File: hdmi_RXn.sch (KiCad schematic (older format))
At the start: 40 parts

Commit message: Fix issues due to different KiCad version
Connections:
- wire segments 205 -> 169

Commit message: Fix caps issues in templates
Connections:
- wire segments 169 -> 171
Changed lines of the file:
@@
 LIBS:hdmi2usb
 LIBS:HDMI2USB-cache
-LIBS:HDMI2USB-pcie-artix7-cache
 EELAYER 25 0
 EELAYER END
 $Descr A3 16535 11693
 encoding utf-8
-Sheet 8 14
+Sheet 1 1
 Title ""
 Date ""
@@
 Wire Wire Line
 	6300 5450 6300 5550
+Wire Wire Line
+	2050 3100 2050 3150
+Wire Wire Line
+	2650 1400 2650 1450
 $EndSCHEMATC

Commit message: Annotate HDMI RX template.
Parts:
- gave numbers to parts that had none: 40

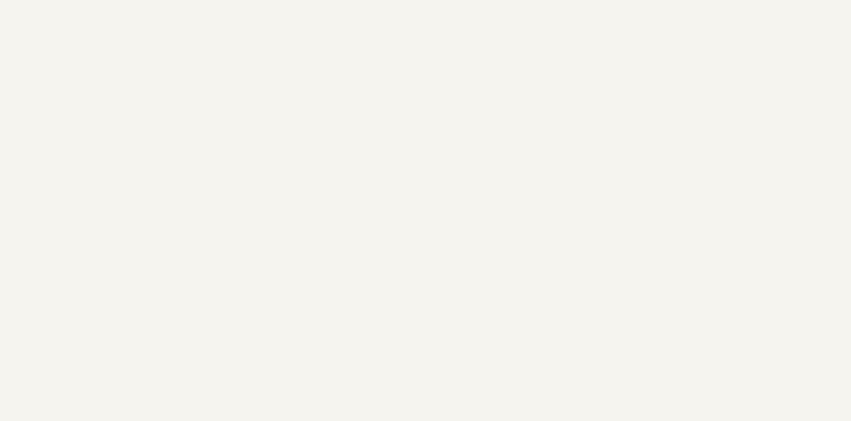
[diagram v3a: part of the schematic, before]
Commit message: Adding warning text.
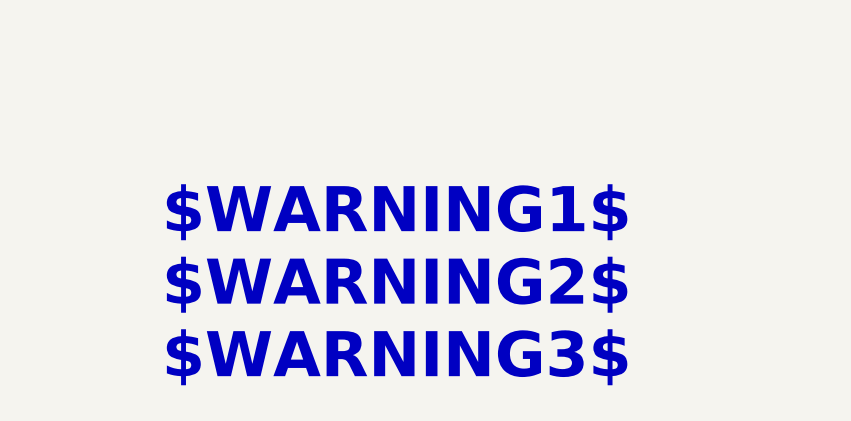
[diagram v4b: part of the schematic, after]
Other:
- note added: "$WARNING1$\n$WARNING2$\n$WARNING3$"
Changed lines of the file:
@@
 LIBS:hdmi2usb
 LIBS:HDMI2USB-cache
+LIBS:hdmi_RXn-cache
 EELAYER 25 0
 EELAYER END
@@
 Wire Wire Line
 	2650 1400 2650 1450
+Text Notes 9945 8285 0    197  ~ 39
+$WARNING1$\n$WARNING2$\n$WARNING3$
 $EndSCHEMATC

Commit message: Add CEC to HDMI headers.
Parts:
- removed P1: CONN_5, symbol CONN_5
- added P1: CONN_01X06, symbol CONN_01X06
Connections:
- wire segments 171 -> 172
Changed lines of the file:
@@
 Text HLabel 6050 5000 0    60   Input ~ 0
 HDMI_$RXn$_PEEN
-$Comp
-L CONN_5 P1
-U 1 1 57C4CA07
-P 6150 6900
-F 0 "P1" V 6100 6900 50  0000 C CNN
-F 1 "CONN_5" V 6200 6900 50  0000 C CNN
-F 2 "" H 6150 6900 60  0000 C CNN
-F 3 "" H 6150 6900 60  0000 C CNN
-	1    6150 6900
-	1    0    0    -1
-$EndComp
 Text Label 4950 6700 0    60   ~ 0
 HDMI_$RXn$_SCL
 Text Label 4950 6800 0    60   ~ 0
 HDMI_$RXn$_SDA
+Text Label 5300 7100 0    60   ~ 0
+VCC3V3
 Text Label 5300 7000 0    60   ~ 0
-VCC3V3
-Text Label 5300 7100 0    60   ~ 0
 GND
 $Comp
@@
 Text Notes 9945 8285 0    197  ~ 39
 $WARNING1$\n$WARNING2$\n$WARNING3$
+$Comp
+L CONN_01X06 P1
+U 1 1 57D665F8
+P 5950 6850
+F 0 "P1" H 6028 6891 50  0000 L CNN
+F 1 "CONN_01X06" H 6028 6800 50  0000 L CNN
+F 2 "" H 5950 6850 50  0000 C CNN
+F 3 "" H 5950 6850 50  0000 C CNN
+	1    5950 6850
+	1    0    0    -1
+$EndComp
+Wire Wire Line
+	5750 6600 4950 6600
+Text Label 4950 6600 0    60   ~ 0
+HDMI_$RXn$_CEC
 $EndSCHEMATC

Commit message: Adding more to the debug header (making it PMOD compatible).
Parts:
- removed P1: CONN_01X06, symbol CONN_01X06
- added P$RXn$1: CONN_02X06, symbol CONN_02X06
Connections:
- net labels added: HDMI_$RXn$_IO0, HDMI_$RXn$_IO1
- wire segments 172 -> 184
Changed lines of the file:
@@
 Text Notes 9945 8285 0    197  ~ 39
 $WARNING1$\n$WARNING2$\n$WARNING3$
-$Comp
-L CONN_01X06 P1
-U 1 1 57D665F8
-P 5950 6850
-F 0 "P1" H 6028 6891 50  0000 L CNN
-F 1 "CONN_01X06" H 6028 6800 50  0000 L CNN
-F 2 "" H 5950 6850 50  0000 C CNN
-F 3 "" H 5950 6850 50  0000 C CNN
-	1    5950 6850
-	1    0    0    -1
-$EndComp
 Wire Wire Line
 	5750 6600 4950 6600
 Text Label 4950 6600 0    60   ~ 0
 HDMI_$RXn$_CEC
+$Comp
+L CONN_02X06 P$RXn$1
+U 1 1 57D66065
+P 6000 6850
+F 0 "P$RXn$1" H 6000 7315 50  0000 C CNN
+F 1 "CONN_02X06" H 6000 7224 50  0000 C CNN
+F 2 "" H 6000 5650 50  0000 C CNN
+F 3 "" H 6000 5650 50  0000 C CNN
+	1    6000 6850
+	1    0    0    -1
+$EndComp
+Wire Wire Line
+	5690 7000 5690 7220
+Wire Wire Line
+	5690 7220 6340 7220
+Wire Wire Line
+	6340 7220 6340 7000
+Wire Wire Line
+	6340 7000 6250 7000
+Connection ~ 5690 7000
+Wire Wire Line
+	5650 7100 5650 7285
+Wire Wire Line
+	5650 7285 6290 7285
+Connection ~ 5650 7100
+Text Label 7050 6700 2    60   ~ 0
+HDMI_$RXn$_IO1
+Text Label 7050 6800 2    60   ~ 0
+HDMI_$RXn$_TXEN
+Text Label 7050 6900 2    60   ~ 0
+HDMI_$RXn$_PEEN
+Wire Wire Line
+	6250 6700 7050 6700
+Wire Wire Line
+	6250 6800 7050 6800
+Wire Wire Line
+	6250 6900 7050 6900
+Wire Wire Line
+	7050 6600 6250 6600
+Text Label 7050 6600 2    60   ~ 0
+HDMI_$RXn$_IO0
+Text HLabel 7050 6600 2    60   BiDi ~ 0
+HDMI_$RXn$_IO0
+Text HLabel 7050 6700 2    60   BiDi ~ 0
+HDMI_$RXn$_IO1
+Wire Wire Line
+	6290 7285 6290 7100
+Wire Wire Line
+	6290 7100 6250 7100
 $EndSCHEMATC

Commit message: Adding footprints to hdmi_RXn schematic.
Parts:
- C$RXn$1, C$RXn$10, C$RXn$11, C$RXn$12, C$RXn$13, C$RXn$14, C$RXn$15, C$RXn$2, C$RXn$3, C$RXn$4, C$RXn$5, C$RXn$6, C$RXn$7, C$RXn$8, C$RXn$9: footprint (none) -> Capacitors_SMD:C_0402
- J$RXn$1: manf# (none) -> 10029449-001RLF
- P$RXn$1: footprint (none) -> Pin_Headers:Pin_Header_Straight_2x06
- R$RXn$1, R$RXn$10, R$RXn$11, R$RXn$12, R$RXn$2, R$RXn$3, R$RXn$4, R$RXn$5, R$RXn$6, R$RXn$7, R$RXn$8, R$RXn$9: footprint (none) -> Resistors_SMD:R_0402
- U$RXn$1: footprint (none) -> Housings_DFN_QFN:QFN-40-1EP_6x6mm_Pitch0.5mm; manf# (none) -> AD8195ACPZ
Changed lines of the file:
@@
 F 0 "U$RXn$1" H 8700 1700 60  0000 C CNN
 F 1 "AD8195" H 8050 2950 60  0000 C CNN
-F 2 "" H 8000 2850 60  0000 C CNN
+F 2 "Housings_DFN_QFN:QFN-40-1EP_6x6mm_Pitch0.5mm" H 8000 2850 60  0001 C CNN
 F 3 "" H 8000 2850 60  0000 C CNN
+F 4 "AD8195ACPZ" H 8050 2850 60  0001 C CNN "manf#"
 	1    8050 2850
 	1    0    0    -1
@@
 F 0 "J$RXn$1" H 4600 4050 60  0000 C CNN
 F 1 "HDMI" V 4900 3000 60  0000 C CNN
-F 2 "" H 4700 3000 60  0000 C CNN
+F 2 "" H 4700 3000 60  0001 C CNN
 F 3 "" H 4700 3000 60  0000 C CNN
+F 4 "10029449-001RLF" H 4750 3000 60  0001 C CNN "manf#"
 	1    4750 3000
 	-1   0    0    -1
@@
 F 0 "R$RXn$5" V 5730 3100 50  0000 C CNN
 F 1 "R" V 5657 3101 50  0000 C CNN
-F 2 "" V 5580 3100 30  0000 C CNN
+F 2 "Resistors_SMD:R_0402" V 5580 3100 30  0001 C CNN
 F 3 "" H 5650 3100 30  0000 C CNN
 	1    5650 3100
@@
 F 0 "D$RXn$2" H 6550 1050 50  0000 C CNN
 F 1 "DIODE" H 6750 950 50  0000 C CNN
-F 2 "" H 6550 950 60  0000 C CNN
+F 2 "" H 6550 950 60  0001 C CNN
 F 3 "" H 6550 950 60  0000 C CNN
 	1    6550 950
@@
 F 0 "D$RXn$3" H 6550 1050 50  0000 C CNN
 F 1 "DIODE" H 6750 1150 50  0000 C CNN
-F 2 "" H 6550 1150 60  0000 C CNN
+F 2 "" H 6550 1150 60  0001 C CNN
 F 3 "" H 6550 1150 60  0000 C CNN
 	1    6550 1150
@@
 $EndComp
 $Comp
-L GND #PWR2
+L GND #PWR01
 U 1 1 57C0819F
 P 7850 4300
-F 0 "#PWR2" H 7850 4050 60  0001 C CNN
+F 0 "#PWR01" H 7850 4050 60  0001 C CNN
 F 1 "GND" H 7850 4150 60  0000 C CNN
 F 2 "" H 7850 4300 60  0000 C CNN
@@
 F 0 "C$RXn$15" H 9100 4100 50  0000 L CNN
 F 1 "C" H 9100 3900 50  0000 L CNN
-F 2 "" H 9088 3850 30  0000 C CNN
+F 2 "Capacitors_SMD:C_0402" H 9088 3850 30  0001 C CNN
 F 3 "" H 9050 4000 60  0000 C CNN
 	1    9050 4000
@@
 F 0 "C$RXn$13" H 6300 1500 50  0000 L CNN
 F 1 "C" H 6800 1400 50  0000 L CNN
-F 2 "" H 6788 1350 30  0000 C CNN
+F 2 "Capacitors_SMD:C_0402" H 6788 1350 30  0001 C CNN
 F 3 "" H 6750 1500 60  0000 C CNN
 	1    6750 1500
@@
 F 0 "C$RXn$14" H 7000 1600 50  0000 L CNN
 F 1 "C" H 7000 1400 50  0000 L CNN
-F 2 "" H 6988 1350 30  0000 C CNN
+F 2 "Capacitors_SMD:C_0402" H 6988 1350 30  0001 C CNN
 F 3 "" H 6950 1500 60  0000 C CNN
 	1    6950 1500
@@
 $EndComp
 $Comp
-L GND #PWR1
+L GND #PWR02
 U 1 1 57C093D2
 P 6850 1800
-F 0 "#PWR1" H 6850 1550 60  0001 C CNN
+F 0 "#PWR02" H 6850 1550 60  0001 C CNN
 F 1 "GND" H 6850 1650 60  0000 C CNN
 F 2 "" H 6850 1800 60  0000 C CNN
@@
 F 0 "R$RXn$9" V 10280 4600 50  0000 C CNN
 F 1 "47K" V 10207 4601 50  0000 C CNN
-F 2 "" V 10130 4600 30  0000 C CNN
+F 2 "Resistors_SMD:R_0402" V 10130 4600 30  0001 C CNN
 F 3 "" H 10200 4600 30  0000 C CNN
 	1    10200 4600
@@
 F 0 "R$RXn$11" V 10430 4600 50  0000 C CNN
 F 1 "47K" V 10357 4601 50  0000 C CNN
-F 2 "" V 10280 4600 30  0000 C CNN
+F 2 "Resistors_SMD:R_0402" V 10280 4600 30  0001 C CNN
 F 3 "" H 10350 4600 30  0000 C CNN
 	1    10350 4600
@@
 F 0 "R$RXn$10" V 10280 5750 50  0000 C CNN
 F 1 "1K" V 10207 5751 50  0000 C CNN
-F 2 "" V 10130 5750 30  0000 C CNN
+F 2 "Resistors_SMD:R_0402" V 10130 5750 30  0001 C CNN
 F 3 "" H 10200 5750 30  0000 C CNN
 	1    10200 5750
@@
 F 0 "R$RXn$12" V 10430 5750 50  0000 C CNN
 F 1 "1K" V 10357 5751 50  0000 C CNN
-F 2 "" V 10280 5750 30  0000 C CNN
+F 2 "Resistors_SMD:R_0402" V 10280 5750 30  0001 C CNN
 F 3 "" H 10350 5750 30  0000 C CNN
 	1    10350 5750
@@
 $EndComp
 $Comp
-L VCC3V3 #PWR3
+L VCC3V3 #PWR03
 U 1 1 57C0DF7C
 P 10200 5300
-F 0 "#PWR3" H 10200 5150 60  0001 C CNN
+F 0 "#PWR03" H 10200 5150 60  0001 C CNN
 F 1 "VCC3V3" H 10200 5440 60  0000 C CNN
 F 2 "" H 10200 5300 60  0000 C CNN
@@
 F 0 "FB$RXn$4" H 5700 3900 50  0000 C CNN
 F 1 "FILTER" H 5700 3700 50  0000 C CNN
-F 2 "" H 5700 3800 60  0000 C CNN
+F 2 "" H 5700 3800 60  0001 C CNN
 F 3 "" H 5700 3800 60  0000 C CNN
 	1    5700 3800
@@
 F 0 "FB$RXn$2" H 1650 2000 50  0000 C CNN
 F 1 "FILTER" H 1650 1750 50  0000 C CNN
-F 2 "" H 1650 1850 60  0000 C CNN
+F 2 "" H 1650 1850 60  0001 C CNN
 F 3 "" H 1650 1850 60  0000 C CNN
 	1    1650 1850
@@
 F 0 "C$RXn$2" H 1700 2250 50  0000 L CNN
 F 1 "10uF" H 2100 2050 50  0000 L CNN
-F 2 "" H 2088 2000 30  0000 C CNN
+F 2 "Capacitors_SMD:C_0402" H 2088 2000 30  0001 C CNN
 F 3 "" H 2050 2150 60  0000 C CNN
 	1    2050 2150
@@
 F 0 "C$RXn$5" H 2200 2250 50  0000 L CNN
 F 1 "0.1uF" H 2400 2050 50  0000 L CNN
-F 2 "" H 2388 2000 30  0000 C CNN
+F 2 "Capacitors_SMD:C_0402" H 2388 2000 30  0001 C CNN
 F 3 "" H 2350 2150 60  0000 C CNN
 	1    2350 2150
@@
 F 0 "C$RXn$8" H 2700 2250 50  0000 L CNN
 F 1 "10nF" H 2700 2050 50  0000 L CNN
-F 2 "" H 2688 2000 30  0000 C CNN
+F 2 "Capacitors_SMD:C_0402" H 2688 2000 30  0001 C CNN
 F 3 "" H 2650 2150 60  0000 C CNN
 	1    2650 2150
@@
 F 0 "C$RXn$3" H 1700 3050 50  0000 L CNN
 F 1 "10uF" H 2100 2850 50  0000 L CNN
-F 2 "" H 2088 2800 30  0000 C CNN
+F 2 "Capacitors_SMD:C_0402" H 2088 2800 30  0001 C CNN
 F 3 "" H 2050 2950 60  0000 C CNN
 	1    2050 2950
@@
 F 0 "C$RXn$6" H 2200 3050 50  0000 L CNN
 F 1 "0.1uF" H 2400 2850 50  0000 L CNN
-F 2 "" H 2388 2800 30  0000 C CNN
+F 2 "Capacitors_SMD:C_0402" H 2388 2800 30  0001 C CNN
 F 3 "" H 2350 2950 60  0000 C CNN
 	1    2350 2950
@@
 F 0 "C$RXn$9" H 2700 3050 50  0000 L CNN
 F 1 "10nF" H 2700 2850 50  0000 L CNN
-F 2 "" H 2688 2800 30  0000 C CNN
+F 2 "Capacitors_SMD:C_0402" H 2688 2800 30  0001 C CNN
 F 3 "" H 2650 2950 60  0000 C CNN
 	1    2650 2950
@@
 F 0 "C$RXn$1" V 1950 1100 50  0000 L CNN
 F 1 "10uF" V 2100 1300 50  0000 L CNN
-F 2 "" H 2088 1100 30  0000 C CNN
+F 2 "Capacitors_SMD:C_0402" H 2088 1100 30  0001 C CNN
 F 3 "" H 2050 1250 60  0000 C CNN
 	1    2050 1250
@@
 F 0 "C$RXn$4" V 2250 1100 50  0000 L CNN
 F 1 "0.1uF" V 2400 1300 50  0000 L CNN
-F 2 "" H 2388 1100 30  0000 C CNN
+F 2 "Capacitors_SMD:C_0402" H 2388 1100 30  0001 C CNN
 F 3 "" H 2350 1250 60  0000 C CNN
 	1    2350 1250
@@
 F 0 "C$RXn$7" V 2550 1100 50  0000 L CNN
 F 1 "0.1uF" V 2700 1300 50  0000 L CNN
-F 2 "" H 2688 1100 30  0000 C CNN
+F 2 "Capacitors_SMD:C_0402" H 2688 1100 30  0001 C CNN
 F 3 "" H 2650 1250 60  0000 C CNN
 	1    2650 1250
@@
 F 0 "C$RXn$10" V 2850 1100 50  0000 L CNN
 F 1 "0.1uF" V 3000 1300 50  0000 L CNN
-F 2 "" H 2988 1100 30  0000 C CNN
+F 2 "Capacitors_SMD:C_0402" H 2988 1100 30  0001 C CNN
 F 3 "" H 2950 1250 60  0000 C CNN
 	1    2950 1250
@@
 F 0 "C$RXn$11" V 3150 1100 50  0000 L CNN
 F 1 "10nF" V 3300 1300 50  0000 L CNN
-F 2 "" H 3288 1100 30  0000 C CNN
+F 2 "Capacitors_SMD:C_0402" H 3288 1100 30  0001 C CNN
 F 3 "" H 3250 1250 60  0000 C CNN
 	1    3250 1250
@@
 F 0 "C$RXn$12" V 3450 1100 50  0000 L CNN
 F 1 "10nF" V 3600 1300 50  0000 L CNN
-F 2 "" H 3588 1100 30  0000 C CNN
+F 2 "Capacitors_SMD:C_0402" H 3588 1100 30  0001 C CNN
 F 3 "" H 3550 1250 60  0000 C CNN
 	1    3550 1250
@@
 F 0 "FB$RXn$3" H 1650 2800 50  0000 C CNN
 F 1 "FILTER" H 1650 2550 50  0000 C CNN
-F 2 "" H 1650 2650 60  0000 C CNN
+F 2 "" H 1650 2650 60  0001 C CNN
 F 3 "" H 1650 2650 60  0000 C CNN
 	1    1650 2650
@@
 F 0 "FB$RXn$1" H 1650 1100 50  0000 C CNN
 F 1 "FILTER" H 1650 850 50  0000 C CNN
-F 2 "" H 1650 950 60  0000 C CNN
+F 2 "" H 1650 950 60  0001 C CNN
 F 3 "" H 1650 950 60  0000 C CNN
 	1    1650 950
@@
 F 0 "R$RXn$6" V 6380 4700 50  0000 C CNN
 F 1 "100K" V 6307 4701 50  0000 C CNN
-F 2 "" V 6230 4700 30  0000 C CNN
+F 2 "Resistors_SMD:R_0402" V 6230 4700 30  0001 C CNN
 F 3 "" H 6300 4700 30  0000 C CNN
 	1    6300 4700
@@
 F 0 "R$RXn$7" V 6380 5300 50  0000 C CNN
 F 1 "100K" V 6307 5301 50  0000 C CNN
-F 2 "" V 6230 5300 30  0000 C CNN
+F 2 "Resistors_SMD:R_0402" V 6230 5300 30  0001 C CNN
 F 3 "" H 6300 5300 30  0000 C CNN
 	1    6300 5300
@@
 F 0 "R$RXn$8" V 6680 5300 50  0000 C CNN
 F 1 "100K" V 6607 5301 50  0000 C CNN
-F 2 "" V 6530 5300 30  0000 C CNN
+F 2 "Resistors_SMD:R_0402" V 6530 5300 30  0001 C CNN
 F 3 "" H 6600 5300 30  0000 C CNN
 	1    6600 5300
@@
 F 0 "Q$RXn$1" H 2800 6500 60  0000 C CNN
 F 1 "FDV301N" H 2800 6400 60  0000 C CNN
-F 2 "" H 2420 6575 60  0000 C CNN
+F 2 "" H 2420 6575 60  0001 C CNN
 F 3 "" H 2420 6575 60  0000 C CNN
 	1    2400 6600
@@
 F 0 "R$RXn$1" V 2180 6900 50  0000 C CNN
 F 1 "100K" V 2107 6901 50  0000 C CNN
-F 2 "" V 2030 6900 30  0000 C CNN
+F 2 "Resistors_SMD:R_0402" V 2030 6900 30  0001 C CNN
 F 3 "" H 2100 6900 30  0000 C CNN
 	1    2100 6900
@@
 F 0 "R$RXn$2" V 2680 6000 50  0000 C CNN
 F 1 "100K" V 2607 6001 50  0000 C CNN
-F 2 "" V 2530 6000 30  0000 C CNN
+F 2 "Resistors_SMD:R_0402" V 2530 6000 30  0001 C CNN
 F 3 "" H 2600 6000 30  0000 C CNN
 	1    2600 6000
@@
 F 0 "Q$RXn$2" H 3400 6400 60  0000 C CNN
 F 1 "FDV301N" H 3400 6300 60  0000 C CNN
-F 2 "" H 3020 6275 60  0000 C CNN
+F 2 "" H 3020 6275 60  0001 C CNN
 F 3 "" H 3020 6275 60  0000 C CNN
 	1    3000 6300
@@
 F 0 "Q$RXn$3" H 4450 6150 60  0000 C CNN
 F 1 "FDV301N" H 4450 6050 60  0000 C CNN
-F 2 "" H 4070 6025 60  0000 C CNN
+F 2 "" H 4070 6025 60  0001 C CNN
 F 3 "" H 4070 6025 60  0000 C CNN
 	1    4050 6050
@@
 F 0 "R$RXn$3" V 3180 5750 50  0000 C CNN
 F 1 "1K" V 3107 5751 50  0000 C CNN
-F 2 "" V 3030 5750 30  0000 C CNN
+F 2 "Resistors_SMD:R_0402" V 3030 5750 30  0001 C CNN
 F 3 "" H 3100 5750 30  0000 C CNN
 	1    3100 5750
@@
 F 0 "D$RXn$1" H 4150 5150 50  0000 C CNN
 F 1 "LED" H 4150 4950 50  0000 C CNN
-F 2 "" H 4150 5050 60  0000 C CNN
+F 2 "" H 4150 5050 60  0001 C CNN
 F 3 "" H 4150 5050 60  0000 C CNN
 	1    4150 5050
@@
 F 0 "R$RXn$4" V 4230 5550 50  0000 C CNN
 F 1 "560R" V 4157 5551 50  0000 C CNN
-F 2 "" V 4080 5550 30  0000 C CNN
+F 2 "Resistors_SMD:R_0402" V 4080 5550 30  0001 C CNN
 F 3 "" H 4150 5550 30  0000 C CNN
 	1    4150 5550
@@
 F 0 "P$RXn$1" H 6000 7315 50  0000 C CNN
 F 1 "CONN_02X06" H 6000 7224 50  0000 C CNN
-F 2 "" H 6000 5650 50  0000 C CNN
+F 2 "Pin_Headers:Pin_Header_Straight_2x06" H 6000 5650 50  0001 C CNN
 F 3 "" H 6000 5650 50  0000 C CNN
 	1    6000 6850

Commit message: Make sure the schematic has leading zeros.
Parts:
- renumbered C$RXn$1 to C$RXn$01, C$RXn$2 to C$RXn$02, C$RXn$3 to C$RXn$03, C$RXn$4 to C$RXn$04, C$RXn$5 to C$RXn$05, C$RXn$6 to C$RXn$06, C$RXn$7 to C$RXn$07, C$RXn$8 to C$RXn$08, C$RXn$9 to C$RXn$09, D$RXn$1 to D$RXn$01, D$RXn$2 to D$RXn$02, D$RXn$3 to D$RXn$03, FB$RXn$1 to FB$RXn$01, FB$RXn$2 to FB$RXn$02, FB$RXn$3 to FB$RXn$03, FB$RXn$4 to FB$RXn$04, P$RXn$1 to P$RXn$01, Q$RXn$1 to Q$RXn$01, Q$RXn$2 to Q$RXn$02, Q$RXn$3 to Q$RXn$03, R$RXn$1 to R$RXn$01, R$RXn$2 to R$RXn$02, R$RXn$3 to R$RXn$03, R$RXn$4 to R$RXn$04, R$RXn$5 to R$RXn$05, R$RXn$6 to R$RXn$06, R$RXn$7 to R$RXn$07, R$RXn$8 to R$RXn$08, R$RXn$9 to R$RXn$09
